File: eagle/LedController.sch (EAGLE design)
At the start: 32 parts, among them IC1 MCP601R, Q1 16MHz, Q5 PMV20EN, X1 2510-, X2 MKDSN1,5/4-5,08

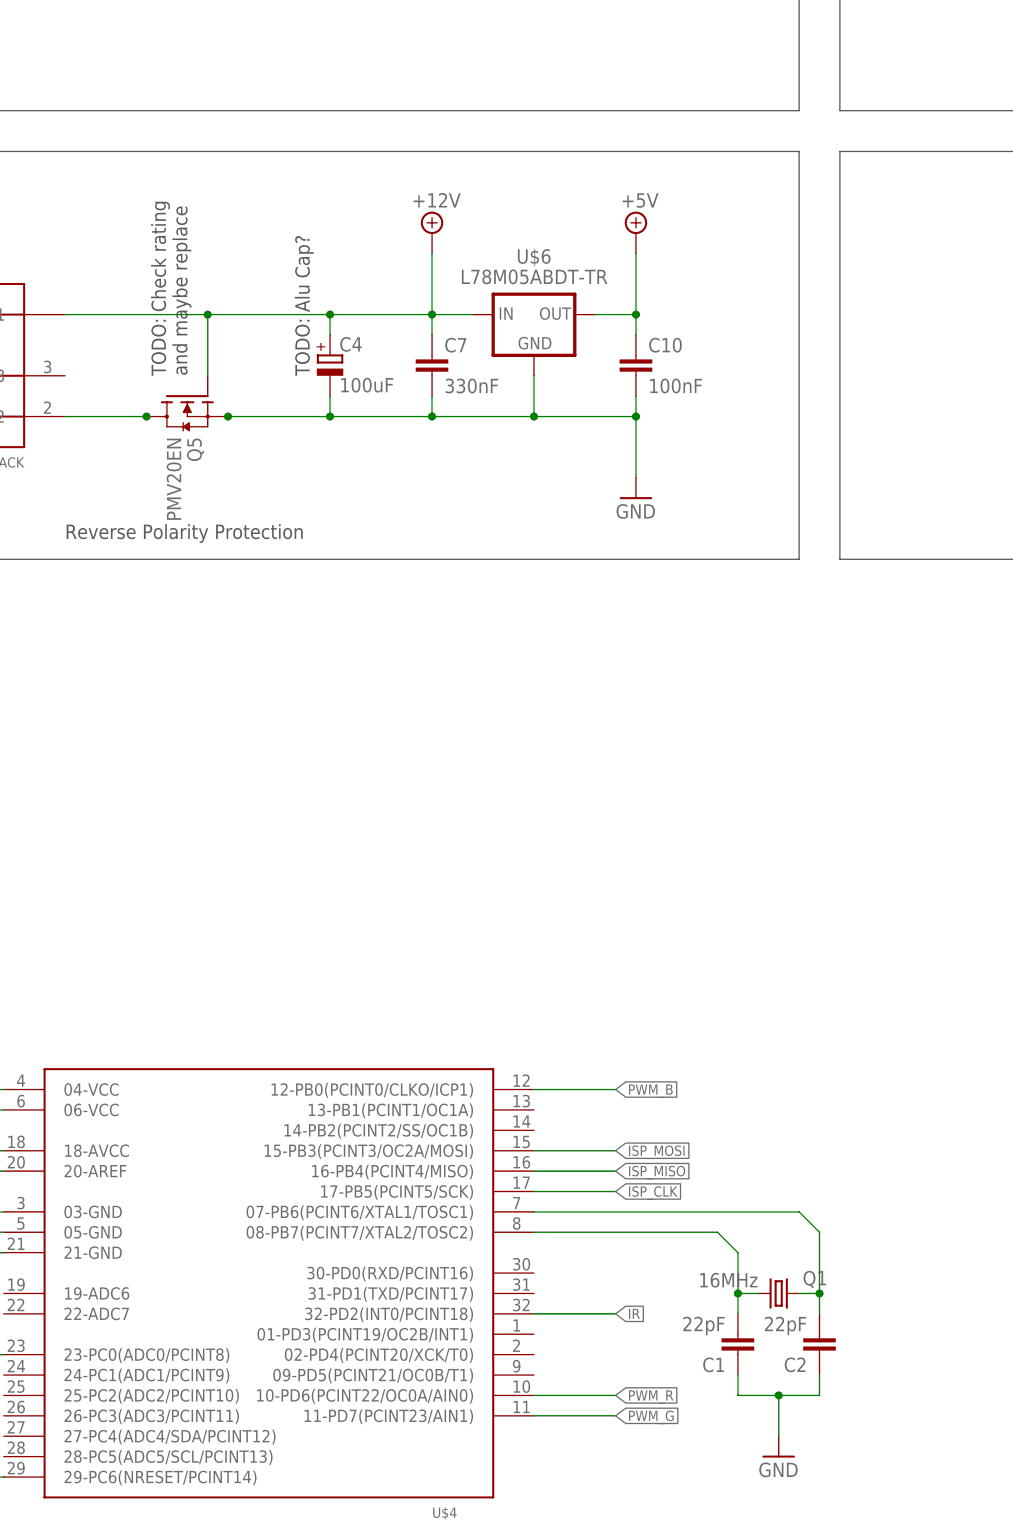
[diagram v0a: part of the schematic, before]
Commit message: Change crystal to SMD type
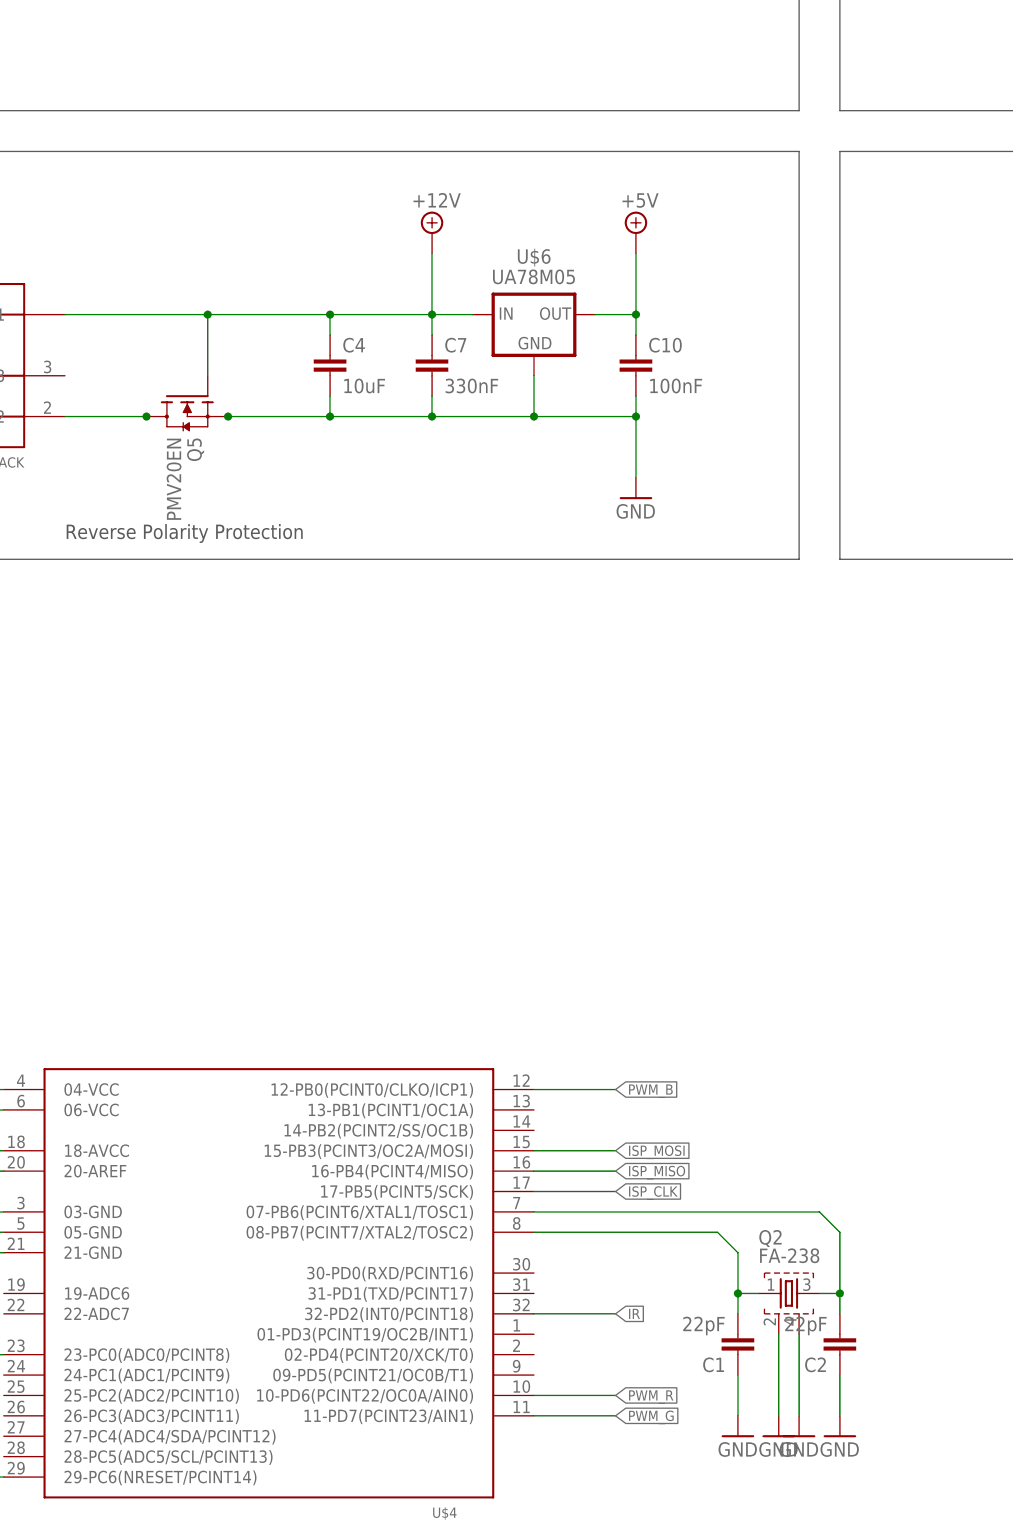
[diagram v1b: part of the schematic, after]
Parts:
- removed Q1: 16MHz, crystal:CRYSTALHC49S
- added Q2: FA-238, LedController:FA-238
- C4: value 100uF -> 10uF; device rcl:CPOL-EU153CLV-0605 -> rcl:C-EUC0805
- U$6: value L78M05ABDT-TR -> UA78M05; device LedController:L78M05ABDT-TR -> LedController:UA78M05
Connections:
- removed net N$2: C1.2, Q1.2
- net +12V: now also C4.1; no longer C4.+
- net GND: now also C4.2, Q2.2, Q2.4; no longer C4.-
- net N$13: now also C1.2, Q2.1
- net N$14: now also Q2.3; no longer Q1.1
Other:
- note removed: "TODO: Alu Cap?"
- note removed: "TODO: Check rating and maybe replace"
- moved on the sheet: C2

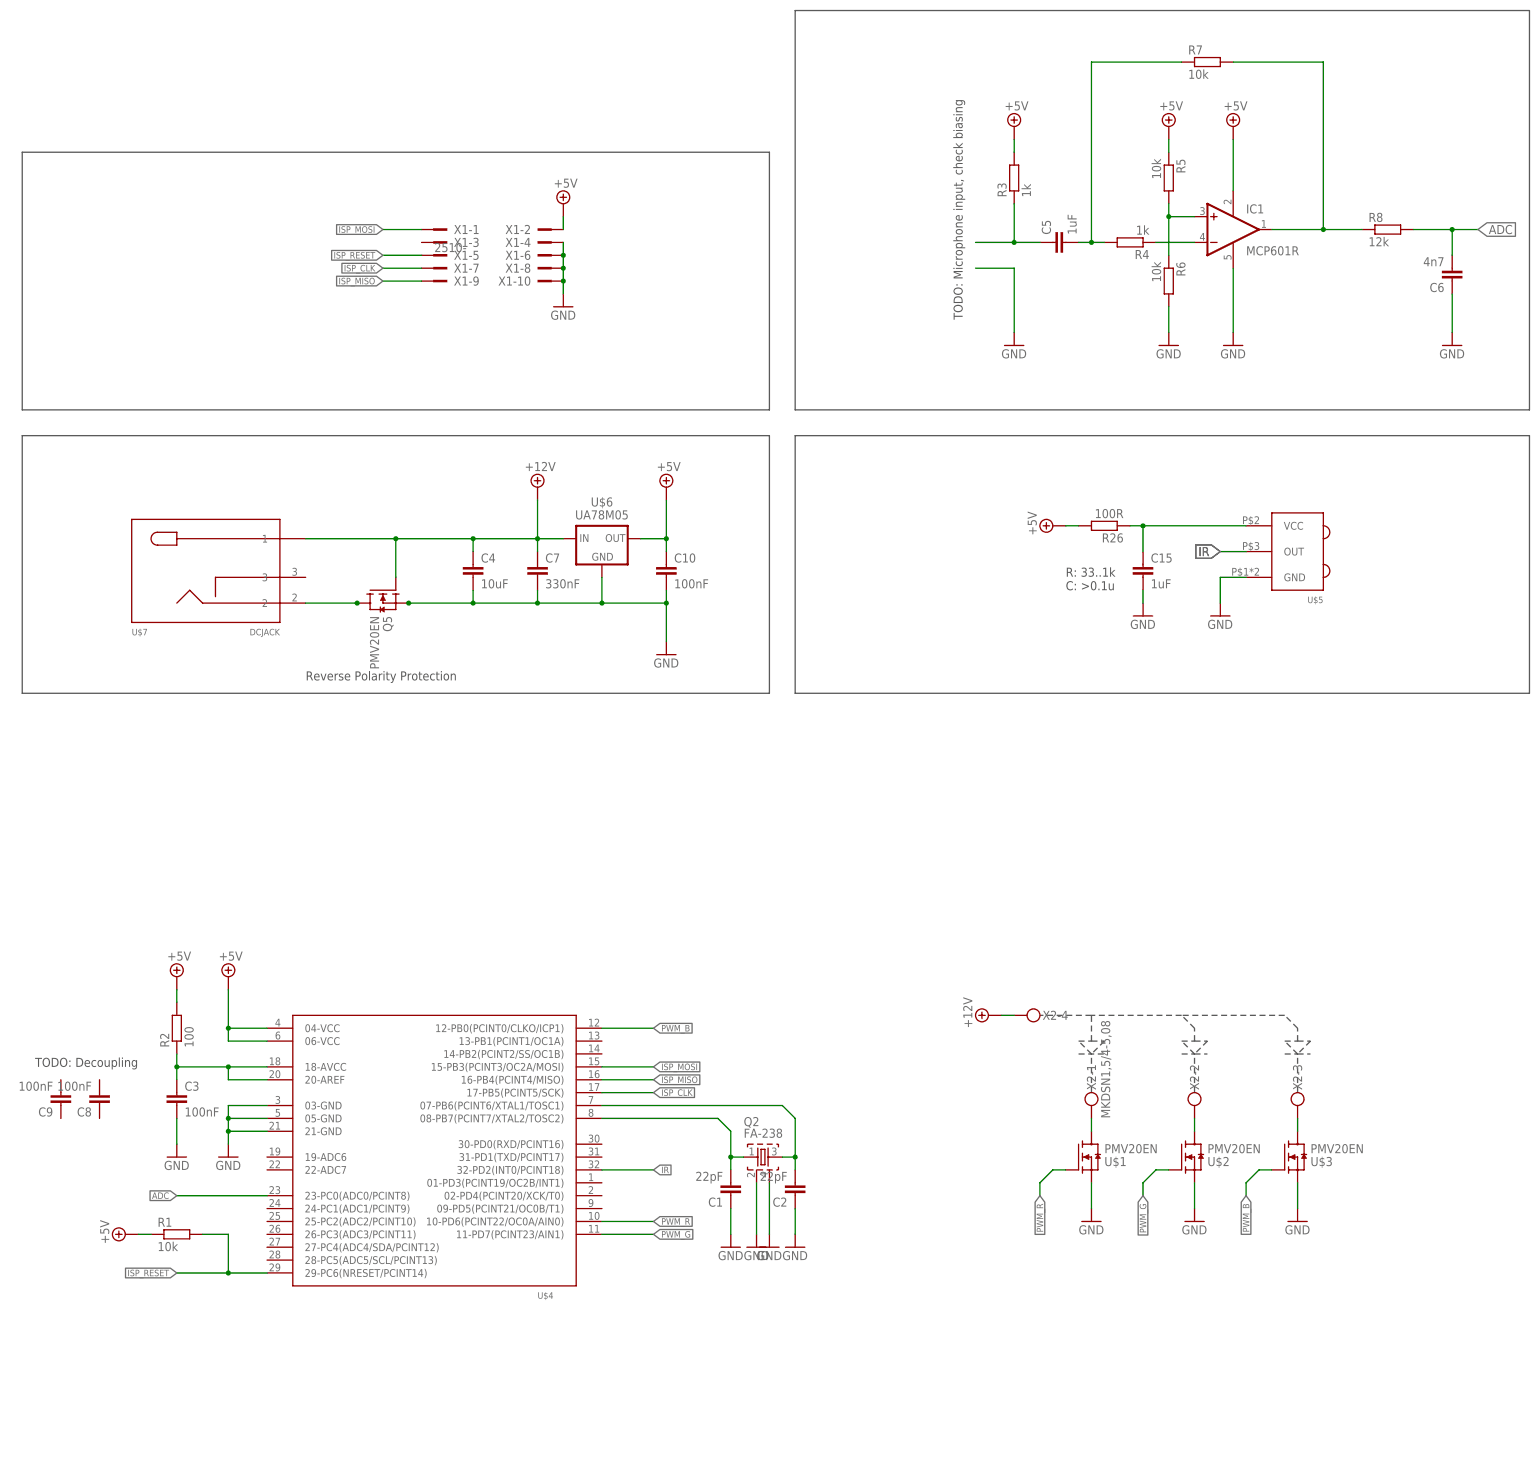
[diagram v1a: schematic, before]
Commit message: Change ISP Connector, layout most things
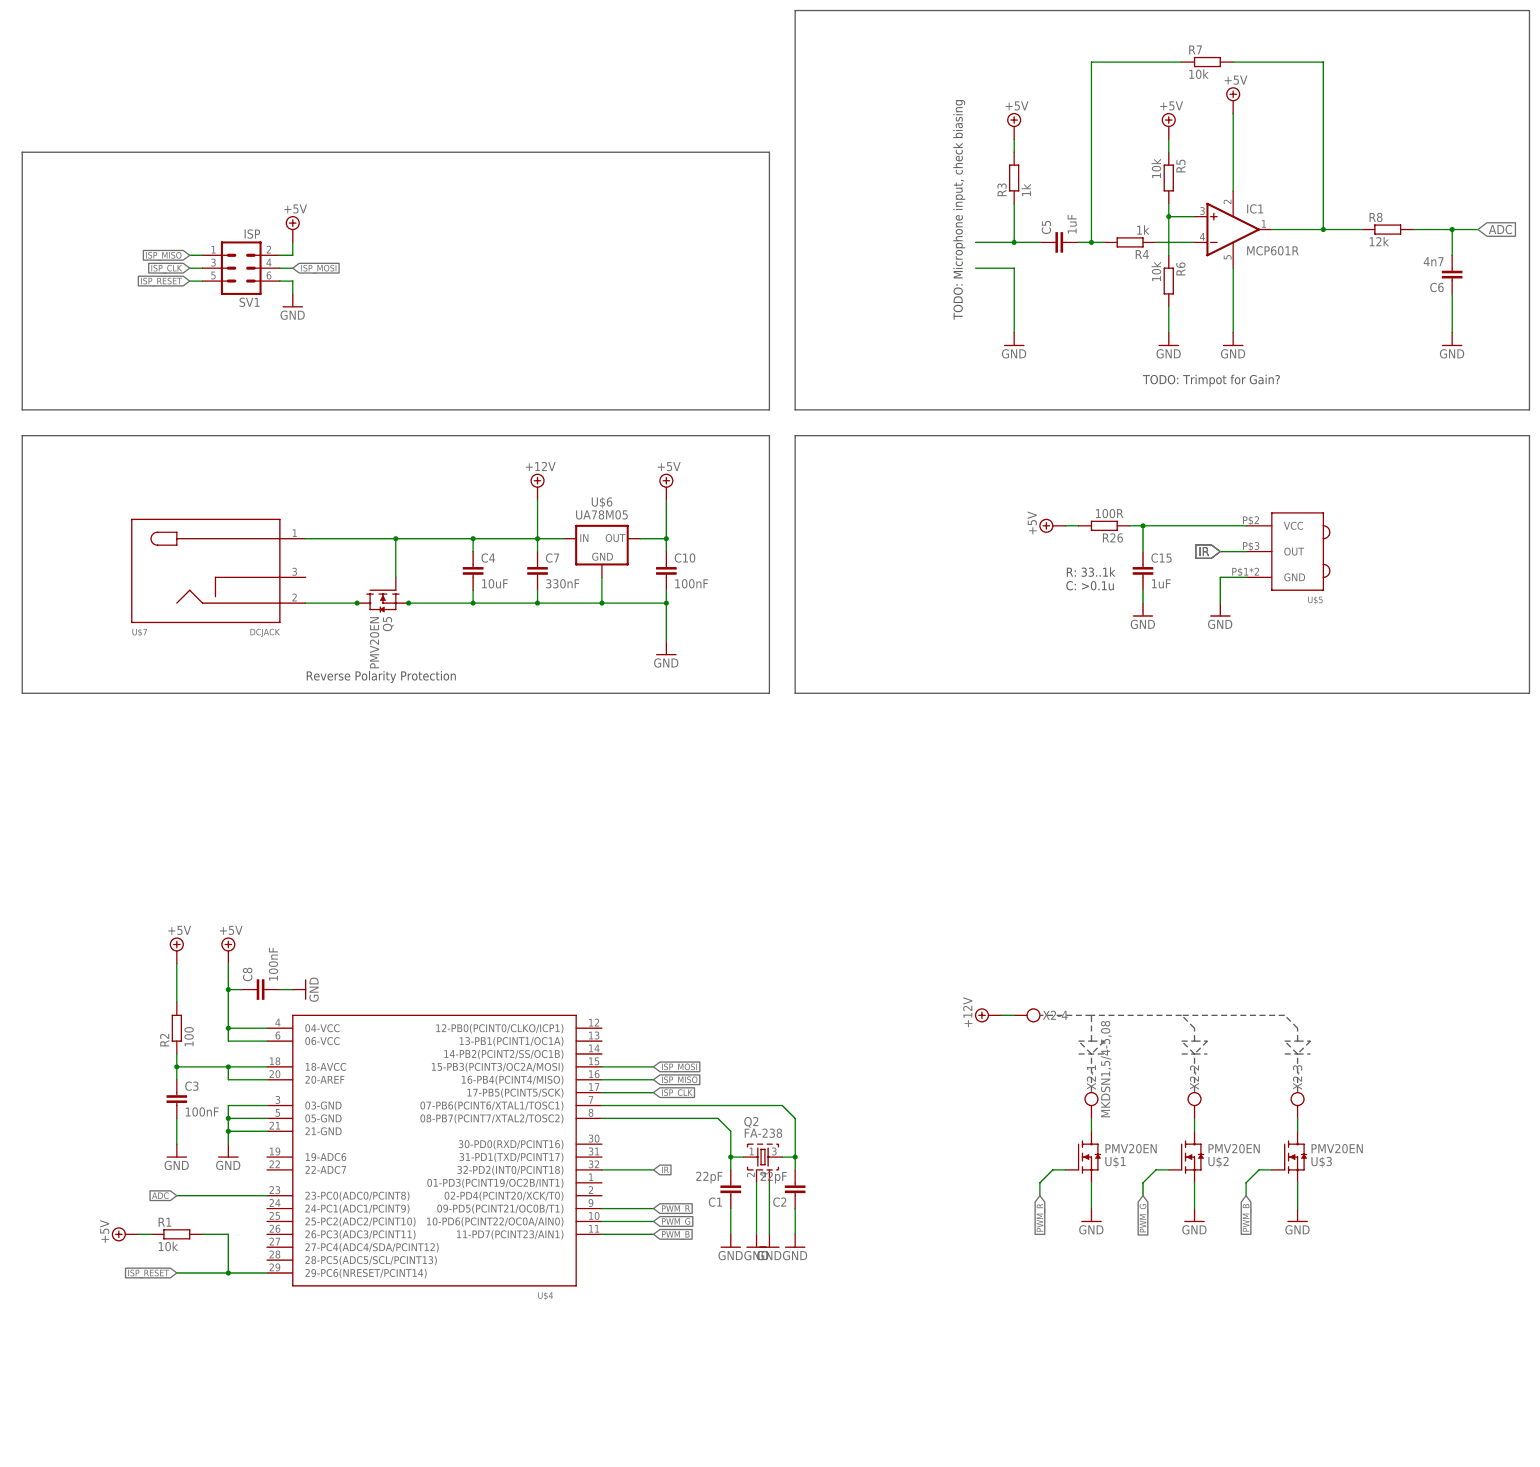
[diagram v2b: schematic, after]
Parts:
- removed C9: 100nF, rcl:C-EUC0805
- removed X1: 2510-, con-3m:2510-
- added SV1: ISP, con-lstb:MA03-2
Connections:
- net +5V: now also C8.1, SV1.2; no longer X1-2.KL
- net GND: now also C8.2, SV1.6; no longer X1-10.KL, X1-4.KL, X1-6.KL, X1-8.KL
- net ISP_CLK: now also SV1.3; no longer X1-7.KL
- net ISP_MISO: now also SV1.1; no longer X1-9.KL
- net ISP_MOSI: now also SV1.4; no longer X1-1.KL
- net ISP_RESET: now also SV1.5; no longer X1-5.KL
- net PWM_B: now also U$4.11-PD7(PCINT23/AIN1); no longer U$4.12-PB0(PCINT0/CLKO/ICP1)
- net PWM_G: now also U$4.10-PD6(PCINT22/OC0A/AIN0); no longer U$4.11-PD7(PCINT23/AIN1)
- net PWM_R: now also U$4.09-PD5(PCINT21/OC0B/T1); no longer U$4.10-PD6(PCINT22/OC0A/AIN0)
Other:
- note added: "TODO: Trimpot for Gain?"
- note removed: "TODO: Decoupling"
- moved on the sheet: C8

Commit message: More relayouting, Framed schematic
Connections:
- net GND: no longer Q2.4
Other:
- moved on the sheet: C1, C10, C15, C2, C3, C4, C5, C6, C7, C8, IC1, Q5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
